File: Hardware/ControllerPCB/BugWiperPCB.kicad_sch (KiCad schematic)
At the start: 15 parts, among them J2 1770924, J3 1776508, J6 1824420000, J7 B2B-XH-AM(LF)(SN), J9 1873207

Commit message: fix schematics and pins for the encoder
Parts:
- C27: footprint Capacitor_SMD:C_0603_1608Metric -> BugWiper_lib:C_0603_1608Metric
- F2, F3: footprint Resistor_SMD:R_1206_3216Metric -> BugWiper_lib:R_1206_3216Metric
- J2: footprint CONN_1814537 -> BugWiper_lib:CONN_1814537
- R27: footprint Resistor_SMD:R_0603_1608Metric -> BugWiper_lib:R_0603_1608Metric
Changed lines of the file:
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@@
       (effects (font (size 1.27 1.27)) (justify right))
     )
-    (property "Footprint" "Resistor_SMD:R_1206_3216Metric" (at 214.63 129.54 0)
+    (property "Footprint" "BugWiper_lib:R_1206_3216Metric" (at 214.63 129.54 0)
       (effects (font (size 1.27 1.27)) (justify left) hide)
     )
@@
       (effects (font (size 1.524 1.524)) (justify left))
     )
-    (property "Footprint" "CONN_1814537" (at 242.57 143.51 0)
+    (property "Footprint" "BugWiper_lib:CONN_1814537" (at 242.57 143.51 0)
       (effects (font (size 1.27 1.27) italic) hide)
     )
@@
       (effects (font (size 1.27 1.27)) (justify right))
     )
-    (property "Footprint" "Resistor_SMD:R_1206_3216Metric" (at 229.87 144.78 0)
+    (property "Footprint" "BugWiper_lib:R_1206_3216Metric" (at 229.87 144.78 0)
       (effects (font (size 1.27 1.27)) (justify left) hide)
     )
@@
       (effects (font (size 1.27 1.27)) (justify left))
     )
-    (property "Footprint" "Capacitor_SMD:C_0603_1608Metric" (at 109.5248 175.26 0)
+    (property "Footprint" "BugWiper_lib:C_0603_1608Metric" (at 109.5248 175.26 0)
       (effects (font (size 1.27 1.27)) hide)
     )
@@
       (effects (font (size 1.27 1.27)) (justify left))
     )
-    (property "Footprint" "Resistor_SMD:R_0603_1608Metric" (at 112.522 171.45 90)
-      (effects (font (size 1.27 1.27)) hide)
-    )
+    (property "Footprint" "BugWiper_lib:R_0603_1608Metric" (at 112.522 171.45 90)
+      (effects (font (size 1.27 1.27)) hide)
+    )

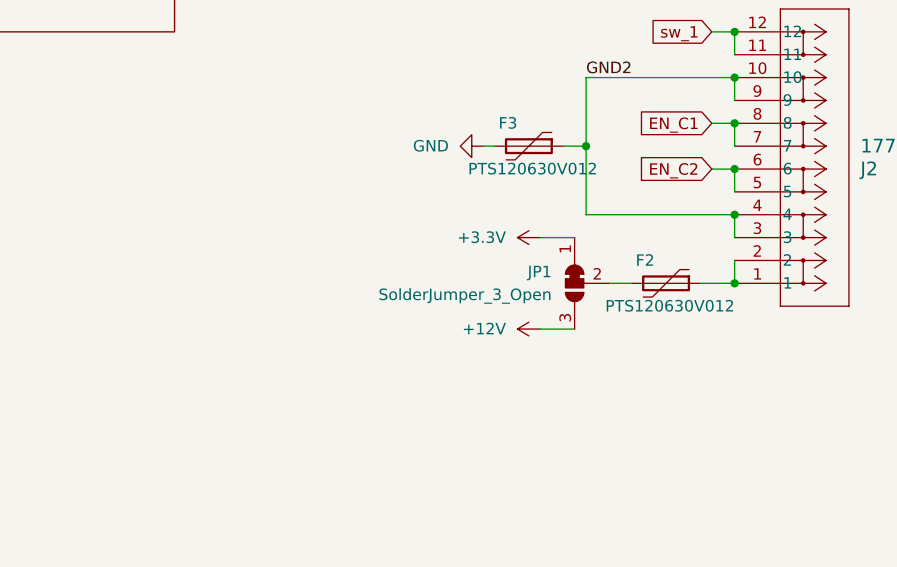
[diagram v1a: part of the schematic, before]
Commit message: update controller PCB: change Encoder filter to 1nF add 0 Ohm resistor for JP1 to BOM
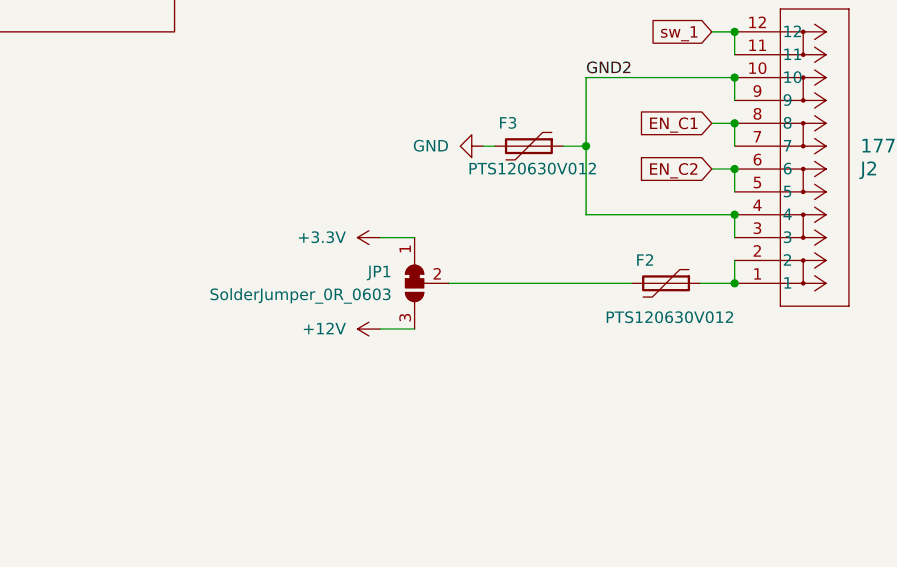
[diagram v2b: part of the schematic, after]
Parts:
- JP1: value SolderJumper_3_Open -> SolderJumper_0R_0603; Manufacturer_Name (none) -> YAGEO; Manufacturer_Part_Number (none) -> RC0603FR-070RL; Mouser Part Number (none) -> 603-RC0603FR-070RL; Mouser Price/Stock (none) -> 0,095€
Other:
- moved on the sheet: JP1
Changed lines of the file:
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@@
   (title_block
     (title "BugWiper 2.0 Controller PCB")
-    (date "2025-01-27")
+    (date "2025-06-02")
+    (rev "V1.1")
     (company "M. Scholjegerdes")
   )
@@
     (stroke (width 0) (type default))
   )
-  (wire (pts (xy 220.98 148.59) (xy 224.79 148.59))
+  (wire (pts (xy 203.2 148.59) (xy 207.01 148.59))
     (stroke (width 0) (type default))
   )
@@
     (stroke (width 0) (type default))
   )
-  (wire (pts (xy 220.98 138.43) (xy 224.79 138.43))
+  (wire (pts (xy 203.2 138.43) (xy 207.01 138.43))
     (stroke (width 0) (type default))
   )
@@
     (stroke (width 0) (type default))
   )
-  (wire (pts (xy 228.6 143.51) (xy 231.14 143.51))
+  (wire (pts (xy 210.82 143.51) (xy 231.14 143.51))
     (stroke (width 0) (type default))
   )
@@
     )
   )
-  (symbol (lib_id "power:+3.3V") (at 220.98 138.43 90) (unit 1)
+  (symbol (lib_id "power:+3.3V") (at 203.2 138.43 90) (unit 1)
     (in_bom yes) (on_board yes) (dnp no) (fields_autoplaced)
-    (property "Reference" "#PWR065" (at 224.79 138.43 0)
-      (effects (font (size 1.27 1.27)) hide)
-    )
-    (property "Value" "+3.3V" (at 217.17 138.43 90)
-      (effects (font (size 1.27 1.27)) (justify left))
-    )
-    (property "Footprint" "" (at 220.98 138.43 0)
-      (effects (font (size 1.27 1.27)) hide)
-    )
-    (property "Datasheet" "" (at 220.98 138.43 0)
+    (property "Reference" "#PWR065" (at 207.01 138.43 0)
+      (effects (font (size 1.27 1.27)) hide)
+    )
+    (property "Value" "+3.3V" (at 199.39 138.43 90)
+      (effects (font (size 1.27 1.27)) (justify left))
+    )
+    (property "Footprint" "" (at 203.2 138.43 0)
+      (effects (font (size 1.27 1.27)) hide)
+    )
+    (property "Datasheet" "" (at 203.2 138.43 0)
       (effects (font (size 1.27 1.27)) hide)
     )
@@
     )
   )
-  (symbol (lib_id "Jumper:SolderJumper_3_Bridged12") (at 224.79 143.51 90) (mirror x) (unit 1)
+  (symbol (lib_id "Jumper:SolderJumper_3_Bridged12") (at 207.01 143.51 90) (mirror x) (unit 1)
     (in_bom no) (on_board yes) (dnp no) (fields_autoplaced)
-    (property "Reference" "JP1" (at 222.25 142.24 90)
-      (effects (font (size 1.27 1.27)) (justify left))
-    )
-    (property "Value" "SolderJumper_3_Open" (at 222.25 144.78 90)
-      (effects (font (size 1.27 1.27)) (justify left))
-    )
-    (property "Footprint" "BugWiper_lib:SolderJumper_R_SMD_0603" (at 224.79 143.51 0)
-      (effects (font (size 1.27 1.27)) hide)
-    )
-    (property "Datasheet" "~" (at 224.79 143.51 0)
-      (effects (font (size 1.27 1.27)) hide)
-    )
-    (property "Alternative MF" "" (at 224.79 143.51 0)
-      (effects (font (size 1.27 1.27)) hide)
-    )
-    (property "Alternative PN" "" (at 224.79 143.51 0)
-      (effects (font (size 1.27 1.27)) hide)
-    )
-    (property "Alternative Price" "" (at 224.79 143.51 0)
-      (effects (font (size 1.27 1.27)) hide)
-    )
-    (property "JLCPCB Part #" "" (at 224.79 143.51 0)
-      (effects (font (size 1.27 1.27)) hide)
-    )
-    (property "JLCPCB Price" "" (at 224.79 143.51 0)
+    (property "Reference" "JP1" (at 204.47 142.24 90)
+      (effects (font (size 1.27 1.27)) (justify left))
+    )
+    (property "Value" "SolderJumper_0R_0603" (at 204.47 144.78 90)
+      (effects (font (size 1.27 1.27)) (justify left))
+    )
+    (property "Footprint" "BugWiper_lib:SolderJumper_R_SMD_0603" (at 207.01 143.51 0)
+      (effects (font (size 1.27 1.27)) hide)
+    )
+    (property "Datasheet" "~" (at 207.01 143.51 0)
+      (effects (font (size 1.27 1.27)) hide)
+    )
+    (property "Alternative MF" "" (at 207.01 143.51 0)
+      (effects (font (size 1.27 1.27)) hide)
+    )
+    (property "Alternative PN" "" (at 207.01 143.51 0)
+      (effects (font (size 1.27 1.27)) hide)
+    )
+    (property "Alternative Price" "" (at 207.01 143.51 0)
+      (effects (font (size 1.27 1.27)) hide)
+    )
+    (property "JLCPCB Part #" "" (at 207.01 143.51 0)
+      (effects (font (size 1.27 1.27)) hide)
+    )
+    (property "JLCPCB Price" "" (at 207.01 143.51 0)
+      (effects (font (size 1.27 1.27)) hide)
+    )
+    (property "Description" "SMD 0 Ohms 100mW 0603 1%" (at 207.01 143.51 0)
+      (effects (font (size 1.27 1.27)) hide)
+    )
+    (property "Manufacturer_Name" "YAGEO" (at 207.01 143.51 0)
+      (effects (font (size 1.27 1.27)) hide)
+    )
+    (property "Manufacturer_Part_Number" "RC0603FR-070RL" (at 207.01 143.51 0)
+      (effects (font (size 1.27 1.27)) hide)
+    )
+    (property "Mouser Part Number" "603-RC0603FR-070RL" (at 207.01 143.51 0)
+      (effects (font (size 1.27 1.27)) hide)
+    )
+    (property "Mouser Price/Stock" "0,095€" (at 207.01 143.51 0)
       (effects (font (size 1.27 1.27)) hide)
     )
@@
       (effects (font (size 1.27 1.27)) (justify right))
     )
-    (property "Value" "PTS120630V012" (at 242.57 146.05 90)
+    (property "Value" "PTS120630V012" (at 242.57 147.32 90)
       (effects (font (size 1.27 1.27)) (justify right))
     )
@@
     )
   )
-  (symbol (lib_id "power:+12V") (at 220.98 148.59 90) (unit 1)
+  (symbol (lib_id "power:+12V") (at 203.2 148.59 90) (unit 1)
     (in_bom yes) (on_board yes) (dnp no) (fields_autoplaced)
-    (property "Reference" "#PWR064" (at 224.79 148.59 0)
-      (effects (font (size 1.27 1.27)) hide)
-    )
-    (property "Value" "+12V" (at 217.17 148.59 90)
-      (effects (font (size 1.27 1.27)) (justify left))
-    )
-    (property "Footprint" "" (at 220.98 148.59 0)
-      (effects (font (size 1.27 1.27)) hide)
-    )
-    (property "Datasheet" "" (at 220.98 148.59 0)
-      (effects (font (size 1.27 1.27)) hide)
-    )
+    (property "Reference" "#PWR064" (at 207.01 148.59 0)
+      (effects (font (size 1.27 1.27)) hide)
+    )
+    (property "Value" "+12V" (at 199.39 148.59 90)
+      (effects (font (size 1.27 1.27)) (justify left))
+    )
+    (property "Footprint" "" (at 203.2 148.59 0)
+      (effects (font (size 1.27 1.27)) hide)
+    )
+    (property "Datasheet" "" (at 203.2 148.59 0)
+      (effects (font (size 1.27 1.27)) hide)
+    )
